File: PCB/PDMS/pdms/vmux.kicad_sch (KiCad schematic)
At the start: 40 parts, among them IC2 74HC4067PW-Q100J, U13 MCP6001-OT

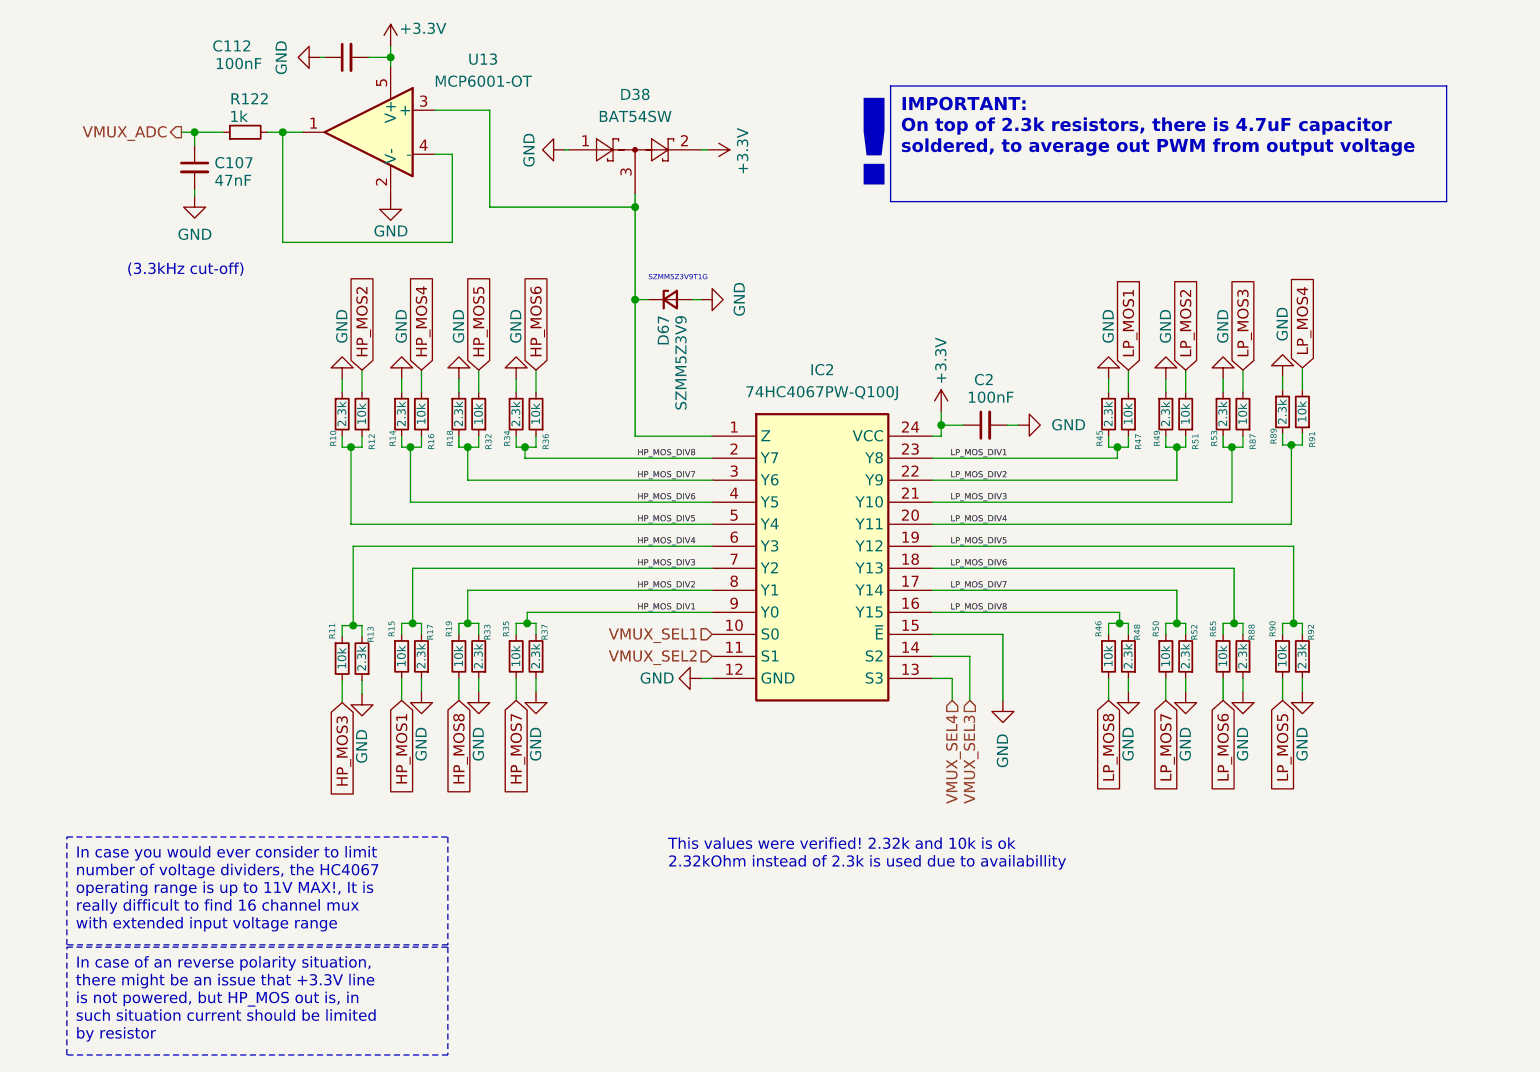
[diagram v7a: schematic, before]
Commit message: Added anit-aliasing filter on Vout - VMux
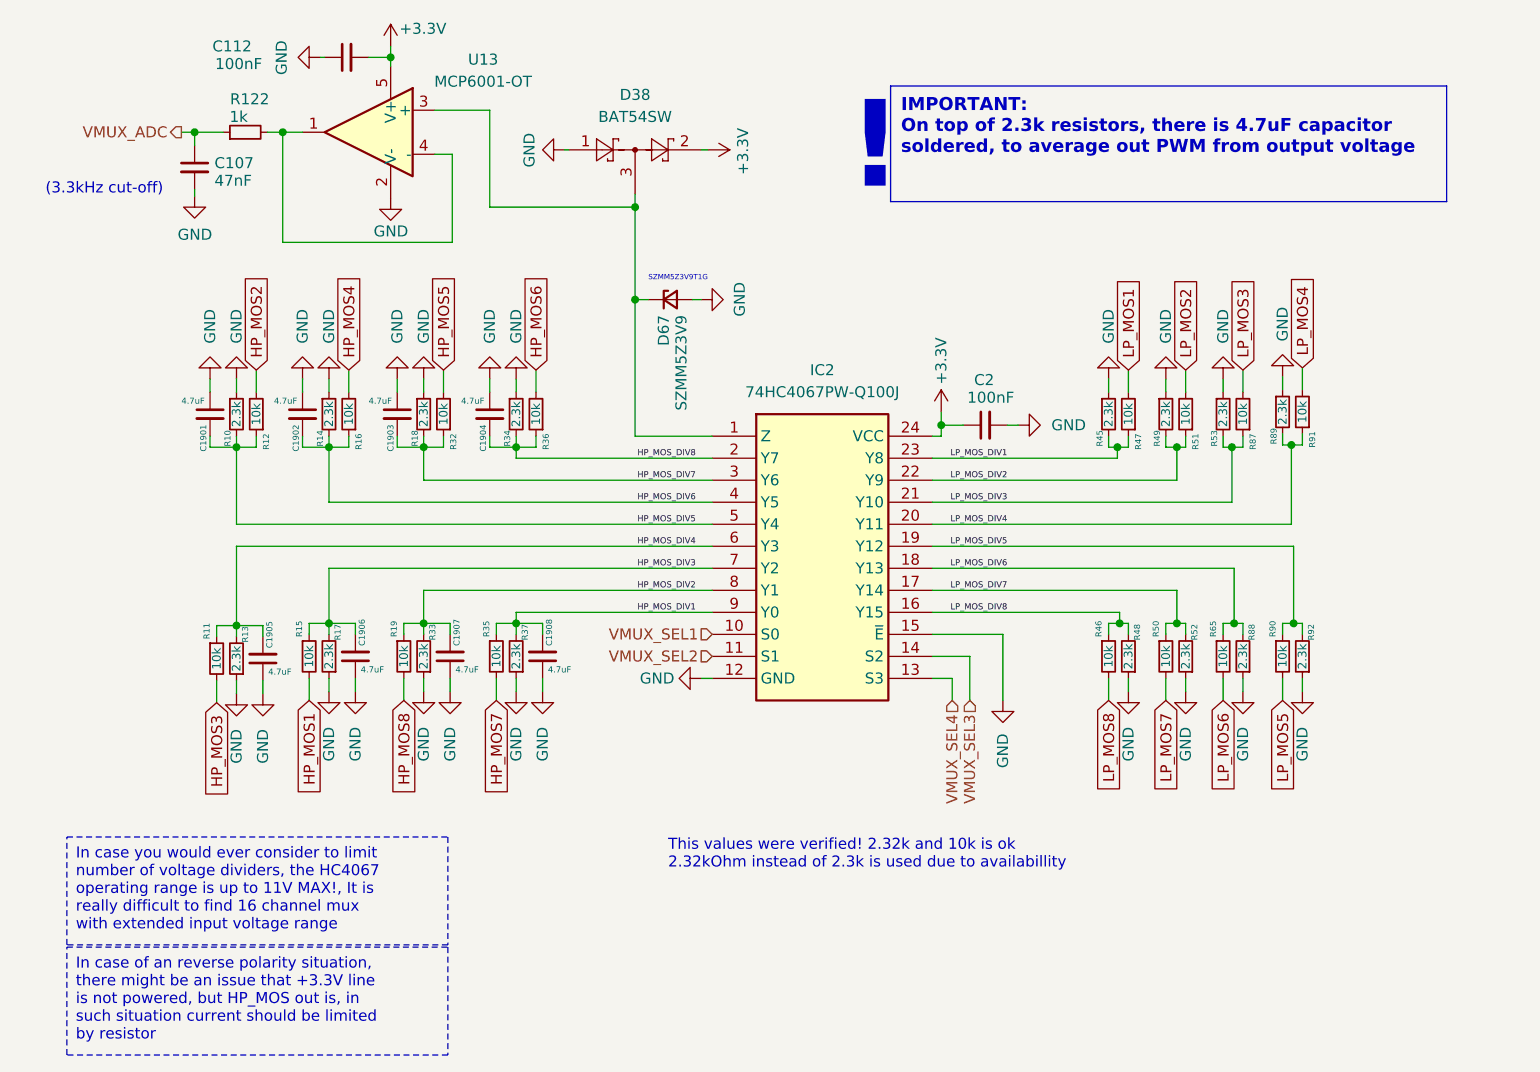
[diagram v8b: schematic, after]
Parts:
- added C1901, C1902, C1903, C1904, C1905, C1906, C1907, C1908: 4.7uF, Capacitor_SMD:C_0402_1005Metric, symbol Device:C_Small
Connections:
- net GND: now also C1901.1, C1902.1, C1903.1, C1904.1, C1905.1, C1906.1, C1907.1, C1908.1
- net HP_MOS_DIV1: now also C1908.2
- net HP_MOS_DIV2: now also C1907.2
- net HP_MOS_DIV3: now also C1906.2
- net HP_MOS_DIV4: now also C1905.2
- net HP_MOS_DIV5: now also C1901.2
- net HP_MOS_DIV6: now also C1902.2
- net HP_MOS_DIV7: now also C1903.2
- net HP_MOS_DIV8: now also C1904.2
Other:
- moved on the sheet: R10, R11, R12, R13, R14, R15, R16, R17, R18, R19, R32, R33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
